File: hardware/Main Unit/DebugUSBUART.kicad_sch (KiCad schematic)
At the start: 14 parts, among them J11 USB4105-GF-A, U10 USBLC6-2SC6, U2 CY7C65223

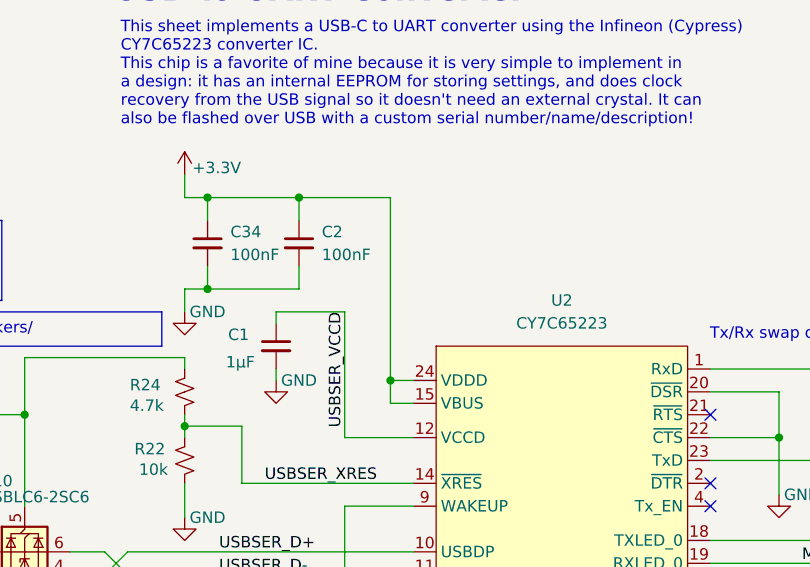
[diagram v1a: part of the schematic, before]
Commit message: Main unit: Add USB port for MCU and 3.3VA rail, start on routing
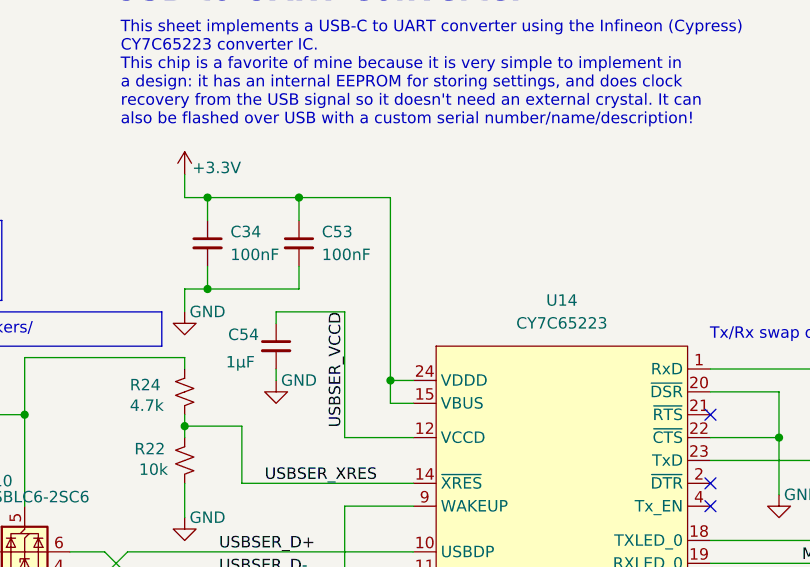
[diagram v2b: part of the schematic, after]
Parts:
- renumbered C2 to C53, C1 to C54, U2 to U14
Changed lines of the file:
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@@
 		(dnp no)
 		(fields_autoplaced yes)
-		(property "Reference" "U2"
+		(property "Reference" "U14"
 			(at 130.81 52.07 0)
 			(effects
@@
 			(project ""
 				(path "/7d91f165-331a-4c48-9d02-ee2a0aa7e94a/435dc57d-0a8b-4ccd-93d5-e5334c096ca6"
-					(reference "U2")
+					(reference "U14")
 					(unit 1)
 				)
@@
 		(on_board yes)
 		(dnp no)
-		(property "Reference" "C1"
+		(property "Reference" "C54"
 			(at 93.726 55.88 0)
 			(effects
@@
 			(project "Main Unit"
 				(path "/7d91f165-331a-4c48-9d02-ee2a0aa7e94a/435dc57d-0a8b-4ccd-93d5-e5334c096ca6"
-					(reference "C1")
+					(reference "C54")
 					(unit 1)
 				)
@@
 		(dnp no)
 		(fields_autoplaced yes)
-		(property "Reference" "C2"
+		(property "Reference" "C53"
 			(at 104.14 44.4562 0)
 			(effects
@@
 			(project "Main Unit"
 				(path "/7d91f165-331a-4c48-9d02-ee2a0aa7e94a/435dc57d-0a8b-4ccd-93d5-e5334c096ca6"
-					(reference "C2")
-					(unit 1)
-				)
+					(reference "C53")
+					(unit 1)
+				)

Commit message: Geographical reannotate
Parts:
- renumbered C34 to C30, C53 to C35, C54 to C37, D4 to D10, D3 to D11, J11 to J16, R22 to R29, R24 to R34, R15 to R50, R19 to R51, R20 to R57, R21 to R58, U10 to U12, U14 to U8
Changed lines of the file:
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@@
 		(dnp no)
 		(fields_autoplaced yes)
-		(property "Reference" "U14"
+		(property "Reference" "U8"
 			(at 130.81 52.07 0)
 			(effects
@@
 			(project "HackerDAQ Main Unit"
 				(path "/7d91f165-331a-4c48-9d02-ee2a0aa7e94a/435dc57d-0a8b-4ccd-93d5-e5334c096ca6"
-					(reference "U14")
+					(reference "U8")
 					(unit 1)
 				)
@@
 		(on_board yes)
 		(dnp no)
-		(property "Reference" "U10"
+		(property "Reference" "U12"
 			(at 66.294 72.136 0)
 			(effects
@@
 			(project "HackerDAQ Main Unit"
 				(path "/7d91f165-331a-4c48-9d02-ee2a0aa7e94a/435dc57d-0a8b-4ccd-93d5-e5334c096ca6"
-					(reference "U10")
+					(reference "U12")
 					(unit 1)
 				)
@@
 		(on_board yes)
 		(dnp no)
-		(property "Reference" "R22"
+		(property "Reference" "R29"
 			(at 83.312 68.58 0)
 			(effects
@@
 			(project "HackerDAQ Main Unit"
 				(path "/7d91f165-331a-4c48-9d02-ee2a0aa7e94a/435dc57d-0a8b-4ccd-93d5-e5334c096ca6"
-					(reference "R22")
+					(reference "R29")
 					(unit 1)
 				)
@@
 		(on_board yes)
 		(dnp no)
-		(property "Reference" "R20"
+		(property "Reference" "R57"
 			(at 194.056 78.74 90)
 			(effects
@@
 			(project "HackerDAQ Main Unit"
 				(path "/7d91f165-331a-4c48-9d02-ee2a0aa7e94a/435dc57d-0a8b-4ccd-93d5-e5334c096ca6"
-					(reference "R20")
+					(reference "R57")
 					(unit 1)
 				)
@@
 		(on_board yes)
 		(dnp no)
-		(property "Reference" "R24"
+		(property "Reference" "R34"
 			(at 82.804 61.468 0)
 			(effects
@@
 			(project "HackerDAQ Main Unit"
 				(path "/7d91f165-331a-4c48-9d02-ee2a0aa7e94a/435dc57d-0a8b-4ccd-93d5-e5334c096ca6"
-					(reference "R24")
+					(reference "R34")
 					(unit 1)
 				)
@@
 		(dnp no)
 		(fields_autoplaced yes)
-		(property "Reference" "C34"
+		(property "Reference" "C30"
 			(at 93.98 44.4562 0)
 			(effects
@@
 			(project "HackerDAQ Main Unit"
 				(path "/7d91f165-331a-4c48-9d02-ee2a0aa7e94a/435dc57d-0a8b-4ccd-93d5-e5334c096ca6"
-					(reference "C34")
+					(reference "C30")
 					(unit 1)
 				)
@@
 		(on_board yes)
 		(dnp no)
-		(property "Reference" "R21"
+		(property "Reference" "R58"
 			(at 187.706 82.55 90)
 			(effects
@@
 			(project "HackerDAQ Main Unit"
 				(path "/7d91f165-331a-4c48-9d02-ee2a0aa7e94a/435dc57d-0a8b-4ccd-93d5-e5334c096ca6"
-					(reference "R21")
+					(reference "R58")
 					(unit 1)
 				)
@@
 		(on_board yes)
 		(dnp no)
-		(property "Reference" "C54"
+		(property "Reference" "C37"
 			(at 93.726 55.88 0)
 			(effects
@@
 			(project "HackerDAQ Main Unit"
 				(path "/7d91f165-331a-4c48-9d02-ee2a0aa7e94a/435dc57d-0a8b-4ccd-93d5-e5334c096ca6"
-					(reference "C54")
+					(reference "C37")
 					(unit 1)
 				)
@@
 		(on_board yes)
 		(dnp no)
-		(property "Reference" "D3"
+		(property "Reference" "D11"
 			(at 182.626 79.248 0)
 			(effects
@@
 			(project "HackerDAQ Main Unit"
 				(path "/7d91f165-331a-4c48-9d02-ee2a0aa7e94a/435dc57d-0a8b-4ccd-93d5-e5334c096ca6"
-					(reference "D3")
+					(reference "D11")
 					(unit 1)
 				)
@@
 		(on_board yes)
 		(dnp no)
-		(property "Reference" "J11"
+		(property "Reference" "J16"
 			(at 38.1 58.42 0)
 			(effects
@@
 			(project "HackerDAQ Main Unit"
 				(path "/7d91f165-331a-4c48-9d02-ee2a0aa7e94a/435dc57d-0a8b-4ccd-93d5-e5334c096ca6"
-					(reference "J11")
+					(reference "J16")
 					(unit 1)
 				)
@@
 		(on_board yes)
 		(dnp no)
-		(property "Reference" "R15"
+		(property "Reference" "R50"
 			(at 43.942 68.326 90)
 			(effects
@@
 			(project "HackerDAQ Main Unit"
 				(path "/7d91f165-331a-4c48-9d02-ee2a0aa7e94a/435dc57d-0a8b-4ccd-93d5-e5334c096ca6"
-					(reference "R15")
+					(reference "R50")
 					(unit 1)
 				)
@@
 		(on_board yes)
 		(dnp no)
-		(property "Reference" "D4"
+		(property "Reference" "D10"
 			(at 173.482 82.804 0)
 			(effects
@@
 			(project "HackerDAQ Main Unit"
 				(path "/7d91f165-331a-4c48-9d02-ee2a0aa7e94a/435dc57d-0a8b-4ccd-93d5-e5334c096ca6"
-					(reference "D4")
+					(reference "D10")
 					(unit 1)
 				)
@@
 		(dnp no)
 		(fields_autoplaced yes)
-		(property "Reference" "C53"
+		(property "Reference" "C35"
 			(at 104.14 44.4562 0)
 			(effects
@@
 			(project "HackerDAQ Main Unit"
 				(path "/7d91f165-331a-4c48-9d02-ee2a0aa7e94a/435dc57d-0a8b-4ccd-93d5-e5334c096ca6"
-					(reference "C53")
+					(reference "C35")
 					(unit 1)
 				)
@@
 		(on_board yes)
 		(dnp no)
-		(property "Reference" "R19"
+		(property "Reference" "R51"
 			(at 43.942 73.914 90)
 			(effects
@@
 			(project "HackerDAQ Main Unit"
 				(path "/7d91f165-331a-4c48-9d02-ee2a0aa7e94a/435dc57d-0a8b-4ccd-93d5-e5334c096ca6"
-					(reference "R19")
-					(unit 1)
-				)
+					(reference "R51")
+					(unit 1)
+				)
